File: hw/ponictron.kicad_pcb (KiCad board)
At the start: 2 copper layers, 71 x 73 mm, 71 parts, among them IC1 SHT40-BD1B-R2, IC2 MAX31328NELB+, IC3 PEC11S-929K-S0015, J1 FFC2B35-24-T, J2 975, J3 M20-7920642R, J4 SM04B-SRSS-TB_LF__SN__P_, Q1 Si1308EDL-T1-GE3, Q2 DMG2305UX-7, Q3 DMG2305UX-7, Q4 2SC5585TL, U1 RaspberryPi_Pico, U2 AS1115-BSST, U3 TDCR1060M

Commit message: Starting board layout
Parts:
- removed A1: ~, RX480E:RX480E
- removed the C10 at (140.0, 85.5)
- removed the C11 at (140.0, 90.8)
- removed C18: 4.7uF, Capacitor_SMD:C_0603_1608Metric
- removed the C7 at (140.0, 83.8)
- removed the C8 at (140.0, 87.2)
- removed D1, D2, D3, D4: MBR0530, Diode_SMD:D_SOD-123
- removed L1: 68 uH, SamacSys_Parts:INDM3225X240N
- removed LED1: WP424IDT, SamacSys_Parts:WP424IDT
- removed the Q1 at (139.9, 72.8)
- removed the Q2 at (139.9, 64.7)
- removed the R11 at (155.2, 93.2)
- removed the R12 at (148.2, 90.0)
- removed the R13 at (159.5, 130.0)
- removed the R14 at (159.5, 132.0)
- removed the R15 at (144.2, 116.0)
- removed the R16 at (156.2, 99.2)
- removed S3, S4, S5, S6, S7, S8: TL3301BF260QJ, SamacSys_Parts:TL3301BF260QJ
- removed the TP1 at (138.5, 98.0)
- added C13: 10uF, Capacitor_SMD:C_0603_1608Metric, F.Cu at (173.8, 13.4)
- added C14: 0.1uF, Capacitor_SMD:C_0603_1608Metric, F.Cu at (173.8, 15.9)
- added C15: 22uF, Capacitor_SMD:C_0603_1608Metric, F.Cu at (177.9, 5.86)
- added C16: 0.1uF, Capacitor_SMD:C_0603_1608Metric, F.Cu at (177.9, 8.37)
- added H1: MountingHole_Pad, MountingHole:MountingHole_2.7mm_M2.5_DIN965_Pad, F.Cu at (142.1, 13.5)
- added H2: MountingHole_Pad, MountingHole:MountingHole_2.7mm_M2.5_DIN965_Pad, F.Cu at (142.1, 19.7)
- added H3: MountingHole_Pad, MountingHole:MountingHole_2.7mm_M2.5_DIN965_Pad, F.Cu at (142.1, 26.0)
- added H4: MountingHole_Pad, MountingHole:MountingHole_2.7mm_M2.5_DIN965_Pad, F.Cu at (142.1, 32.2)
- added J10: B3B-PH-SM4-TB_LF__SN_, B3B-PH-SM4-TB_LF__SN_:JST_B3B-PH-SM4-TB_LF__SN_, F.Cu at (133.0, 22.4)
- added J11: 470531000, 0470531000:CONN_SD-47053-001_H10p00_MOL, F.Cu at (184.7, 30.0)
- added J13: FC68148S, FC68148S:FC68148S_CLF, F.Cu at (167.1, 26.3)
- added J4: B3B-PH-SM4-TB_LF__SN_, B3B-PH-SM4-TB_LF__SN_:JST_B3B-PH-SM4-TB_LF__SN_, F.Cu at (133.0, -13.8)
- added J5: 470531000, 0470531000:CONN_SD-47053-001_H10p00_MOL, F.Cu at (184.7, 22.3)
- added J6: Conn_01x10, Connector_PinHeader_2.54mm:PinHeader_1x10_P2.54mm_Vertical, F.Cu at (205.8, -22.4)
- added J7: B3B-PH-SM4-TB_LF__SN_, B3B-PH-SM4-TB_LF__SN_:JST_B3B-PH-SM4-TB_LF__SN_, F.Cu at (133.0, -4.79)
- added J8: B3B-PH-SM4-TB_LF__SN_, B3B-PH-SM4-TB_LF__SN_:JST_B3B-PH-SM4-TB_LF__SN_, F.Cu at (133.0, 4.25)
- added J9: B3B-PH-SM4-TB_LF__SN_, B3B-PH-SM4-TB_LF__SN_:JST_B3B-PH-SM4-TB_LF__SN_, F.Cu at (133.0, 13.3)
- added Q3: 2SC5585TL, SamacSys_Parts:2SC5585TL, F.Cu at (154.0, 43.0)
- added R10: 47kΩ, Resistor_SMD:R_0603_1608Metric_Pad0.98x0.95mm_HandSolder, F.Cu at (165.3, 45.8)
- added R18: 1kΩ, Resistor_SMD:R_0603_1608Metric_Pad0.98x0.95mm_HandSolder, F.Cu at (169.7, 35.8)
- added R19: 40kΩ, Resistor_SMD:R_0603_1608Metric_Pad0.98x0.95mm_HandSolder, F.Cu at (169.7, 38.3)
- added R21: 66kΩ, Resistor_SMD:R_0603_1608Metric_Pad0.98x0.95mm_HandSolder, F.Cu at (169.7, 40.8)
- added R22: 2SA2018TL, 2SA2018TL:TRANS_2SA2018_ROM, F.Cu at (153.3, 38.4)
- added R23: 2SA2018TL, 2SA2018TL:TRANS_2SA2018_ROM, F.Cu at (156.6, 38.4)
- added R24: 40kΩ, Resistor_SMD:R_0603_1608Metric_Pad0.98x0.95mm_HandSolder, F.Cu at (169.7, 43.3)
- added R25: 40kΩ, Resistor_SMD:R_0603_1608Metric_Pad0.98x0.95mm_HandSolder, F.Cu at (169.7, 45.8)
- added R3: 1kΩ, Resistor_SMD:R_0603_1608Metric_Pad0.98x0.95mm_HandSolder, F.Cu at (161.0, 40.8)
- added R4: 47kΩ, Resistor_SMD:R_0603_1608Metric_Pad0.98x0.95mm_HandSolder, F.Cu at (161.0, 43.3)
- added R5: 47kΩ, Resistor_SMD:R_0603_1608Metric_Pad0.98x0.95mm_HandSolder, F.Cu at (161.0, 45.8)
- added R6: 47kΩ, Resistor_SMD:R_0603_1608Metric_Pad0.98x0.95mm_HandSolder, F.Cu at (165.3, 35.8)
- added R7: 10kΩ, Resistor_SMD:R_0603_1608Metric_Pad0.98x0.95mm_HandSolder, F.Cu at (165.3, 38.3)
- added R8: 47kΩ, Resistor_SMD:R_0603_1608Metric_Pad0.98x0.95mm_HandSolder, F.Cu at (165.3, 40.8)
- added R9: 47kΩ, Resistor_SMD:R_0603_1608Metric_Pad0.98x0.95mm_HandSolder, F.Cu at (165.3, 43.3)
- added TP2: ADC_VREF, TestPoint:TestPoint_Pad_1.5x1.5mm, F.Cu at (149.9, 38.1)
- added U4: MPM3550EGLE, Package_LGA:MPS_LGA-18-10EP_12x12mm_P3.3mm, F.Cu at (182.1, 40.8)
- added U5: DMP4015SSSQ-13, DMP4015SSSQ-13:SO8_DIO, F.Cu at (184.1, 14.7)
- C1: value 4.7uF -> 10uF
- C10: renamed from C13; value 1uF -> 0.1uF
- C11: renamed from C16; value 1uF -> 0.1uF
- C12, C17, C4, C5, C9: value 1uF -> 10uF
- C2: value 1uF -> 0.1uF
- C3, C6: value 4.7uF -> 0.1uF
- C7: renamed from C14; value 1uF -> 0.1uF
- C8: renamed from C15; value 1uF -> 0.1uF
- J1: value FFC2B35-24-T -> RJCSE538001; footprint SamacSys_Parts:FFC2B3524T -> RJCSE538001:AMPHENOL_RJCSE538001
- J2: value 975 -> Conn_01x10; footprint SamacSys_Parts:975 -> Connector_PinHeader_2.54mm:PinHeader_1x10_P2.54mm_Vertical; moved to F.Cu
- J3: value M20-7920642R -> MSD-11-A; footprint SamacSys_Parts:M207920642R -> MSD_11_A:CUI_MSD-11-A
- LS1: value CSS-I4B20-SMT-TR -> CPT-1203-03-SMT-TR; footprint SamacSys_Parts:CSSI4B20SMTTR -> CPT_1203_03_SMT_TR:XDCR_CPT-1203-03-SMT-TR
- R1: value 10kΩ -> 4.7kΩ
- R2: value 0.47Ω -> 2kΩ
- R20: renamed from R6; value 180Ω -> 40kΩ
- S1, S2: value RKB2SJK250SMTR_LFS -> TL3301BF260QJ; footprint SamacSys_Parts:RKB2SJK250SMTRLFS -> SamacSys_Parts:TL3301BF260QJ
- TP1: renamed from TP2; value TestPoint -> Bootsel
- TP3: value TestPoint -> RTC_INT
- U1: moved to F.Cu
- U2: value AS1115-BSST -> LM358M; footprint Package_SO:QSOP-24_3.9x8.7mm_P0.635mm -> LM358M:8-SOP_OSI
- U3: value TDCR1060M -> MCP4725A1T-E/CH; footprint footprints:TDCG1060M_VIS -> MCP4725A1T_E_CH:SOT-23-6_MC_MCH
- moved J2 150.2 mm to (271.0, 8.96), turned to 0 degrees
- moved J1 146.4 mm to (278.1, 67.0), turned to 180 degrees
- moved LS1 146.2 mm to (233.5, -15.2)
- moved S2 100.7 mm to (153.5, 31.8), turned to 0 degrees
- moved U2 94.8 mm to (184.2, 8.00), turned to 0 degrees
- moved C17 92.1 mm to (177.9, 10.9)
- moved J3 89.8 mm to (257.3, 74.6), turned to 180 degrees
- moved C2 86.0 mm to (169.8, 8.37), turned to 0 degrees
- moved C6 81.7 mm to (173.8, 5.86), turned to 0 degrees
- moved C12 78.8 mm to (173.8, 10.9), turned to 0 degrees
- moved C9 77.9 mm to (173.8, 8.37), turned to 0 degrees
- moved C3 75.1 mm to (169.8, 10.9), turned to 0 degrees
- moved U3 74.8 mm to (141.7, 37.7), turned to 0 degrees
- moved C1 70.3 mm to (169.8, 5.86), turned to 0 degrees
- moved C4 68.4 mm to (169.8, 13.4), turned to 0 degrees
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- renumbered H1 to H5, H2 to H6, H3 to H7, H4 to H8, J4 to J12, Q4 to Q1, Q3 to Q2, R3 to R11, R4 to R12, R5 to R13, R7 to R14, R8 to R15, R9 to R16, R10 to R17
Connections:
- C1 pad 1: +3.3V -> GND
- C1 pad 2: GND -> +3.3V
- C12 pad 1: GND -> +3.3V
- C12 pad 2: Net-(J1-VDD) -> GND
- C2 pad 2: /VGL -> +3.3V
- C3 pad 1: Net-(D3-A) -> GND
- C3 pad 2: Net-(D1-A) -> +12V
- C4 pad 2: /VGH -> +12V
- C5 pad 2: Net-(J1-VGL/NC) -> +3.3V
- C9 pad 1: GND -> +3.3V
- C9 pad 2: Net-(J1-VSH2) -> GND
- IC2 pad 3: /RTC_INT -> Net-(IC2-~{INT}/SQW)
- IC3 pad D1: /Enc_D -> Net-(IC3-COM)
- J1 pad 2: /GDR -> unconnected-(J1-Pad2)
- J1 pad 3: /RESE -> unconnected-(J1-Pad3)
- J1 pad 4: Net-(J1-VGL/NC) -> unconnected-(J1-Pad4)
- J1 pad 5: Net-(J1-VSH2) -> GND
- J1 pad 6: unconnected-(J1-TSCL-Pad6) -> Net-(U2-OUT1)
- J1 pad 8: GND -> unconnected-(J1-Pad8)
- J12 pad 1: /SCL -> GND
- J12 pad 2: /SDA -> +3.3V
- J12 pad 3: +3.3V -> /SDA
- J12 pad 4: GND -> /SCL
- J2 pad 1: Net-(J2-+) -> GND
- J2 pad 2: unconnected-(J2-NC-Pad2) -> +3.3V
- J2 pad 3: GND -> unconnected-(J2-Pin_3-Pad3)
- Q1 pad 3: Net-(D4-A) -> Net-(Q1-C)
- R1 pad 1: /GDR -> +3.3V
- R1 pad 2: GND -> /onewire
- R13 pad 2: /RTC_INT -> Net-(IC2-~{INT}/SQW)
- R16 pad 2: /SCL -> /SDA
- R17 pad 2: /SDA -> /SCL
- R2 pad 1: /RESE -> Net-(U2-OUT1)
- R2 pad 2: GND -> Net-(U2-IN1(-))
- S1 pad 1: unconnected-(S1-COM_1-Pad1) -> /BUT1
- S1 pad 2: Net-(S1-COM_2) -> unconnected-(S1-Pad2)
- S2 pad 1: unconnected-(S2-COM_1-Pad1) -> /BUT2
- S2 pad 2: +3.3V -> unconnected-(S2-Pad2)
- S2 pad 4: Net-(S2-NO_2) -> GND
- TP3 pad 1: Net-(U1-GPIO20) -> Net-(IC2-~{INT}/SQW)
- U1 pad 11: /GP8 -> /msdDAT1
- U1 pad 12: /GP9 -> /msdDAT2
- U1 pad 14: /GP14 -> /msdCS
- U1 pad 15: /IRQ -> /msdDet
- U1 pad 16: /ANODE_L3 -> /FAN
- U1 pad 17: /ANODE_L1_L2 -> /BUT1
- U1 pad 19: Net-(U1-GPIO14) -> /BUT2
- U1 pad 20: /RF1 -> /GP15
- U1 pad 21: /EinkBUSY -> /DispRST
- U1 pad 22: /EinkRESET -> /DispCS
- U1 pad 26: Net-(U1-GPIO20) -> /MISO
- U1 pad 27: /EinkCS -> /DispCS
- U1 pad 29: /DC -> /Buzzer
- U1 pad 30: Net-(S1-COM_2) -> unconnected-(U1-RUN-Pad30)
- U1 pad 33: /AGND -> GNDA
- U1 pad 35: /ADC_VREF -> Net-(U1-ADC_VREF)
- U1 pad 4: /Buzzer -> /Enc_E
- U1 pad 5: /RTC_INT -> /onewire
- U2 pad 1: /SDA -> Net-(U2-OUT1)
- U2 pad 2: Net-(U2-DIG0) -> Net-(U2-IN1(-))
- U2 pad 3: Net-(U2-DIG1) -> Net-(U2-IN1(+))
- U2 pad 4: Net-(U2-DIG2) -> GND
- U2 pad 5: Net-(U2-DIG3) -> unconnected-(U2-IN2(+)-Pad5)
- U2 pad 6: GND -> unconnected-(U2-IN2(-)-Pad6)
- U2 pad 8: unconnected-(U2-DIG5-Pad8) -> +12V
- U3 pad 1: Net-(U2-DIG0) -> Net-(U2-IN1(+))
- U3 pad 2: Net-(U2-DIG1) -> GND
- U3 pad 3: Net-(U2-SEGD) -> +3.3V
- U3 pad 4: Net-(U3-CC_L1_L2) -> /SDA
- U3 pad 5: Net-(U2-SEGE) -> /SCL
- U3 pad 6: Net-(U2-DIG2) -> Net-(U3-A0)
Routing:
- net /Enc_D: track 111.1 -> 0.00 mm
- net GND: track 109.5 -> 16.0 mm, vias 21 -> 6
- net /SDA: track 67.7 -> 0.00 mm, vias 4 -> 0
- net /SCL: track 62.2 -> 0.00 mm, vias 3 -> 0
- net Net-(U2-SEGG): track 59.1 -> 0.00 mm, vias 1 -> 0
- net /RF1: track 47.0 -> 0.00 mm
- net /Enc_E: track 46.4 -> 0.00 mm, vias 1 -> 0
- net /DC: track 42.1 -> 0.00 mm, vias 1 -> 0
- net Net-(U2-SEGA): track 37.7 -> 0.00 mm, vias 2 -> 0
- net Net-(U2-SEGB): track 36.2 -> 0.00 mm
- net Net-(U2-SEGF): track 33.7 -> 0.00 mm, vias 1 -> 0
- net /EinkCS: track 32.6 -> 0.00 mm, vias 1 -> 0
- net Net-(U2-SEGC): track 30.6 -> 0.00 mm, vias 1 -> 0
- net Net-(U2-DIG0): track 29.4 -> 0.00 mm
- net Net-(U2-SEGE): track 28.2 -> 0.00 mm, vias 1 -> 0
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
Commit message: Create board layout
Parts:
- J2, J6: footprint Connector_PinHeader_2.54mm:PinHeader_1x10_P2.54mm_Vertical -> Connector_PinSocket_2.54mm:PinSocket_1x10_P2.54mm_Vertical
- U4: footprint Package_LGA:MPS_LGA-18-10EP_12x12mm_P3.3mm -> MPM3550EGLE:MPM3550EGLE
- moved J1 212.4 mm to (67.0, 91.3), turned to -90 degrees
- moved LS1 157.2 mm to (102.2, 71.2), turned to 90 degrees
- moved H6 151.0 mm to (64.0, 49.0), turned to -135 degrees
- moved J2 139.3 mm to (152.7, 82.6), turned to 180 degrees
- moved J3 137.6 mm to (121.5, 52.7)
- moved H5 136.6 mm to (64.0, 116.0), turned to -135 degrees
- moved U2 131.2 mm to (82.0, 90.3), turned to 90 degrees
- moved C15 129.1 mm to (105.7, 113.0), turned to -90 degrees
- moved C1 128.6 mm to (82.8, 100.5)
- moved J11 125.6 mm to (65.3, 69.1), turned to 90 degrees
- moved U5 124.6 mm to (96.0, 102.8), turned to 180 degrees
- moved C2 124.6 mm to (86.0, 100.5), turned to 180 degrees
- moved J5 121.3 mm to (72.8, 69.1), turned to 90 degrees
- moved J13 119.3 mm to (82.7, 110.6), turned to 180 degrees
- moved C13 116.2 mm to (101.5, 104.2), turned to -90 degrees
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- renumbered R22 to Q2, Q2 to Q3, R23 to Q4, Q3 to Q5, R24 to R22, R25 to R23
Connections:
- J2 pad 10: unconnected-(J2-Pin_10-Pad10) -> /BlitePWM
- J2 pad 3: unconnected-(J2-Pin_3-Pad3) -> /DispD/C
- J6 pad 2: /MISO -> GND
- J6 pad 3: /MOSI -> GND
- J6 pad 4: /SCK -> /MOSI
- J6 pad 5: /GP7 -> /MISO
- J6 pad 6: /GP6 -> /SCK
- J6 pad 7: /GP15 -> /GP7
- J6 pad 8: /SCL -> /GP6
- J6 pad 9: /SDA -> +3.3V
- U1 pad 11: /msdDAT1 -> /DispD/C
- U1 pad 12: /msdDAT2 -> /BlitePWM
- U1 pad 14: /msdCS -> /BUT2
- U1 pad 15: /msdDet -> /BUT1
- U1 pad 16: /FAN -> /msdDet
- U1 pad 17: /BUT1 -> /DispRST
- U1 pad 19: /BUT2 -> /msdDAT2
- U1 pad 20: /GP15 -> /msdDAT1
- U1 pad 21: /DispRST -> /MISO
- U1 pad 26: /MISO -> /msdCS
- U1 pad 27: /DispCS -> /Buzzer
- U1 pad 29: /Buzzer -> /FAN
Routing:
- net /MOSI: track 0.00 -> 141.2 mm
- net GND: track 16.0 -> 143.7 mm, vias 6 -> 27
- net /SCL: track 0.00 -> 111.0 mm, vias 0 -> 2
- net /SDA: track 0.00 -> 109.9 mm, vias 0 -> 2
- net /SCK: track 0.00 -> 97.6 mm, vias 0 -> 1
- net GNDA: track 0.00 -> 77.5 mm
- net /MISO: track 9.79 -> 82.5 mm, vias 1 -> 0
- net /ADC2: track 0.00 -> 67.1 mm, vias 0 -> 2
- net +12V: track 0.00 -> 66.2 mm
- net /GP6: track 0.00 -> 58.9 mm
- net /GP7: track 0.00 -> 58.9 mm
- net /onewire: track 0.00 -> 58.9 mm
- net /BUT1: track 0.00 -> 54.2 mm, vias 0 -> 2
- net /ADC1: track 0.00 -> 53.3 mm, vias 0 -> 2
- net /FAN: track 0.00 -> 52.5 mm, vias 0 -> 1
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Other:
- board size 71 x 73 mm -> 121 x 73 mm
- board text added: "3.3V"
- board text added: "GND"
- board text added: "GP6"
- board text added: "GP7"
- board text added: "MISO"
- board text added: "MOSI"
- board text added: "SCK"
- board text added: "ponictron v1 Ben Bokser"
- board text removed: "persuasive_waker v3 Ben Bokser"

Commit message: Making changes to schematic based on feedback
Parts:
- added L1: SRR6028-3R9Y, SRR6028-3R9Y:IND_BOURNS_SRR6028, F.Cu at (88.2, 25.7)
- added U4: AP63203WU-7, AP63203WU-7:AP63203WU-7_DIO, F.Cu at (86.3, 32.5)
- added U5: NC7WZ14P6X, NC7WZ14P6X:SC70-6_ONS, F.Cu at (91.3, 32.1)
- renumbered C17 to C15, C15 to C16, C16 to C17, Q3 to Q1, U5 to U6
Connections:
- C14 pad 1: GND -> Net-(U4-SW)
- C14 pad 2: +12V -> Net-(U4-BST)
- C16 pad 1: GND -> Net-(Q1-D)
- C16 pad 2: Net-(Q3-D) -> GND
- LS1 pad N: Net-(Q4-C) -> Net-(LS1-PadN)
- LS1 pad P: Net-(Q1-C) -> Net-(U5-Y2)
- Q1 pad 3: Net-(Q3-D) -> Net-(Q1-D)

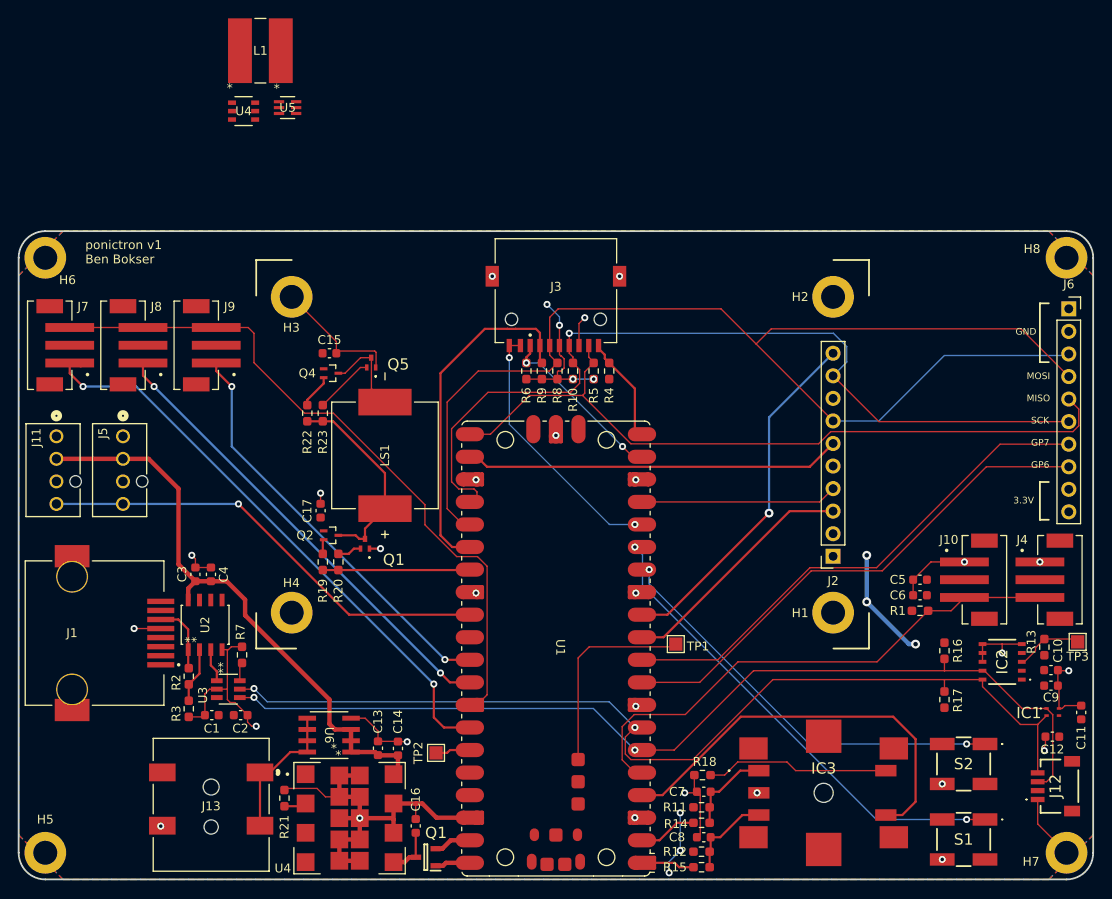
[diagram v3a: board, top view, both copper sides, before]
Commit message: Fix trace widths, update 3D models
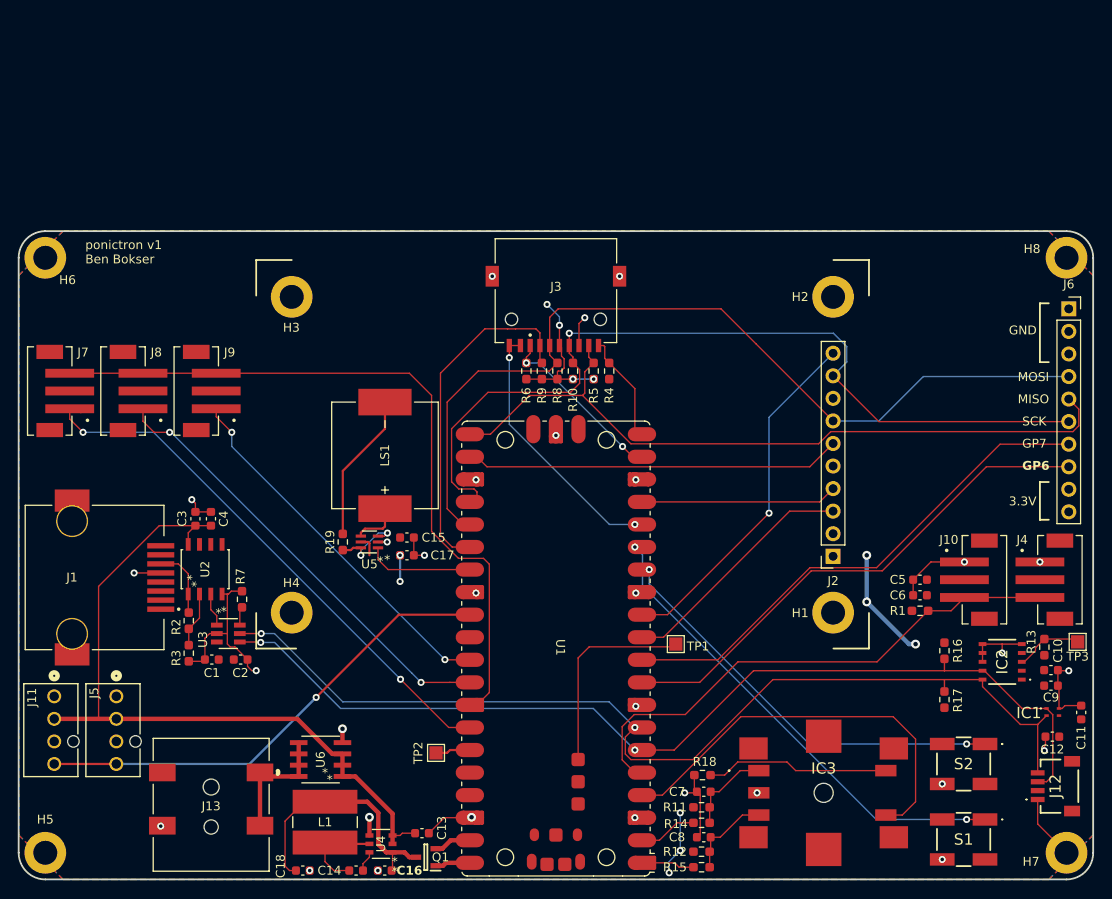
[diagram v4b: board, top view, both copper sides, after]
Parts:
- removed the Q1 at (100.0, 81.2)
- removed Q2, Q4: 2SA2018TL, 2SA2018TL:TRANS_2SA2018_ROM
- removed Q5: 2SC5585TL, SamacSys_Parts:2SC5585TL
- removed R20, R22, R23: 40kΩ, Resistor_SMD:R_0603_1608Metric_Pad0.98x0.95mm_HandSolder
- removed R21: 66kΩ, Resistor_SMD:R_0603_1608Metric_Pad0.98x0.95mm_HandSolder
- removed the U4 at (98.3, 112.1)
- added C18: 22uF, Capacitor_SMD:C_0603_1608Metric, F.Cu at (93.0, 118.0)
- R19: value 40kΩ -> 100Ω
- moved L1 87.2 mm to (95.5, 112.5), turned to -90 degrees
- moved U4 84.0 mm to (101.8, 115.0), turned to 180 degrees
- moved U5 49.8 mm to (100.5, 81.0), turned to 180 degrees
- moved J5 29.3 mm to (72.0, 98.4)
- moved J11 29.3 mm to (65.0, 98.4)
- moved C15 22.5 mm to (104.7, 80.5)
- moved C14 14.5 mm to (99.0, 118.0), turned to 0 degrees
- moved C17 10.9 mm to (104.7, 82.5), turned to 180 degrees
- moved C13 10.8 mm to (106.4, 113.8), turned to 180 degrees
- moved C1 6.26 mm to (82.8, 94.2)
- moved C2 6.26 mm to (86.0, 94.2)
- moved C3 6.26 mm to (80.9, 78.4)
- moved C4 6.26 mm to (82.7, 78.4)
- moved J1 6.26 mm to (67.0, 85.0)
- moved R3 6.26 mm to (80.2, 93.5)
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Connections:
- R19 pad 1: /Buzzer -> Net-(U5-A2)
- R19 pad 2: Net-(Q2-B) -> Net-(LS1-PadN)
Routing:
- net GND: track 143.7 -> 85.8 mm, vias 27 -> 30
- net /MOSI: track 141.2 -> 102.0 mm
- net Net-(Q1-D): track 0.00 -> 28.9 mm
- net Net-(Q1-C): track 22.7 -> 0.00 mm
- net Net-(LS1-PadN): track 0.00 -> 16.8 mm
- net +12V: track 66.2 -> 82.9 mm
- net Net-(U4-SW): track 0.00 -> 10.4 mm
- net Net-(Q4-C): track 10.1 -> 0.00 mm
- net Net-(U5-A2): track 0.00 -> 8.52 mm, vias 0 -> 2
- net Net-(Q5-B): track 6.71 -> 0.00 mm
- net Net-(Q3-D): track 5.53 -> 0.00 mm
- net Net-(U5-Y2): track 0.00 -> 5.39 mm
- net +3.3V: track 37.3 -> 42.6 mm, vias 10 -> 12
- net /ADC0: track 47.7 -> 42.5 mm
- net /Buzzer: track 17.4 -> 13.0 mm
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
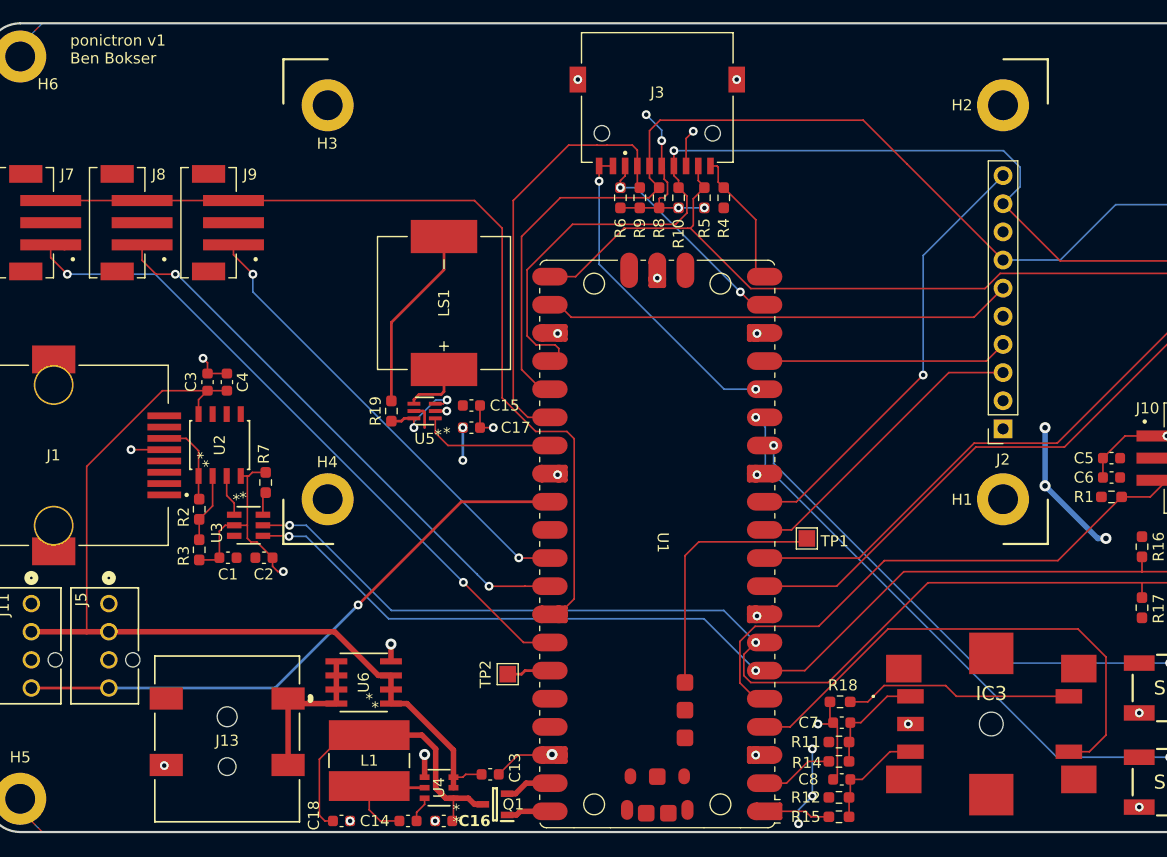
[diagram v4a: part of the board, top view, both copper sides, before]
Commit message: Change display thru-holes to insert mounts
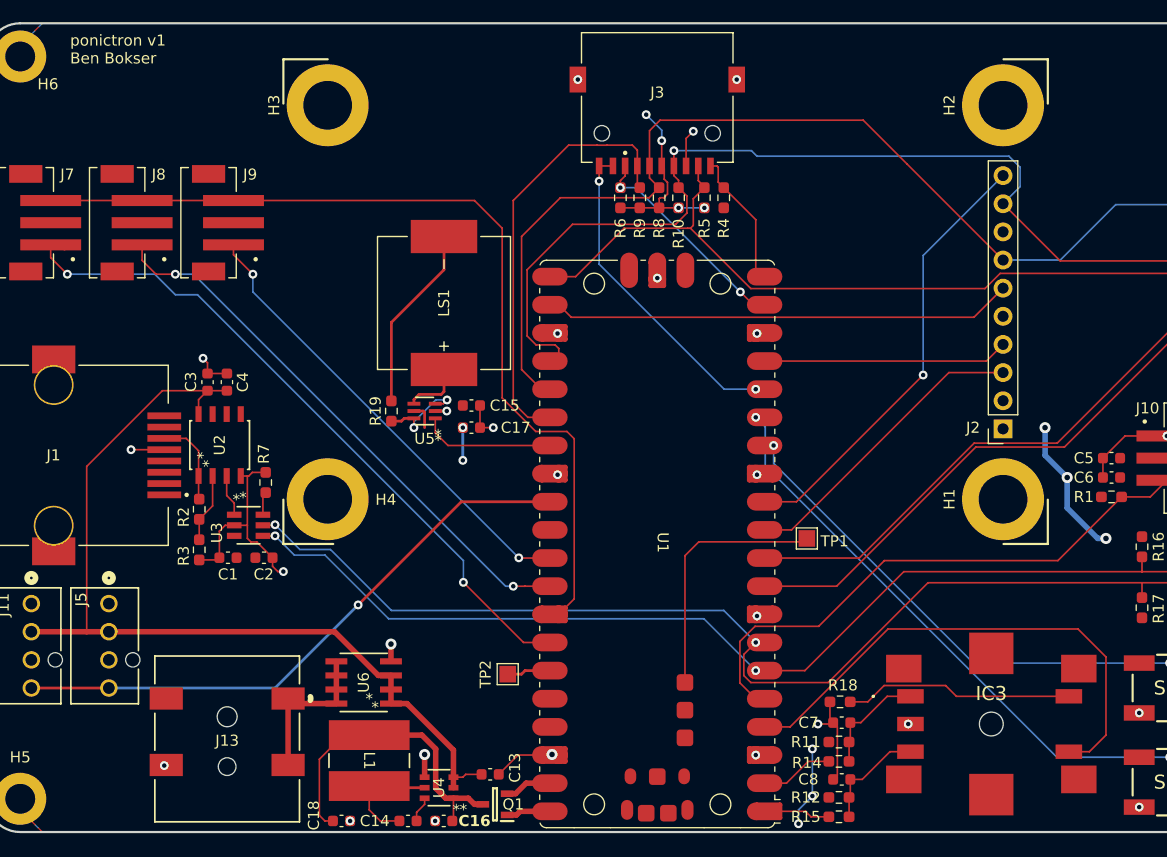
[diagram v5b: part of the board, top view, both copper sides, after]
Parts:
- H1, H2, H3, H4: footprint MountingHole:MountingHole_2.7mm_M2.5_DIN965_Pad -> 78614015360:WE-SMSA_78614015360
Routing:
- net /ADC2: track 62.8 -> 64.0 mm
